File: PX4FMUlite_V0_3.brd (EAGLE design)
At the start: 48.6 x 34.9 mm, 145 parts, among them J2 DF13-4P-1.25V, J201 DF13C-6P-1.25V, J202 DF13C-6P-1.25V, J203 DF13C-6P-1.25V, J3 DF13C-4P-1.25V, J302 DF13C-4P-1.25V, J401 DF13C-4P-1.25V, J403 DF13C-7P-1.25V, J405 DF13C-4P-1.25V, J802 DF13C-3P-1.25V, M3_MOUNT1101 MOUNT-HOLE3.1MM, M3_MOUNT1102 MOUNT-HOLE3.1MM, M3_MOUNT1103 MOUNT-HOLE3.1MM, M3_MOUNT1104 MOUNT-HOLE3.1MM, U101 STM32F4X7VX, U2 MAX3051, U401 MAX3051, X101 3.2x2.5 mm / 24 MHz / 15 ppm

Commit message: More...
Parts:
- moved U$801 6.11 mm to (7.92, 7.11)
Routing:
- net V_SERVO: track 2.50 -> 9.15 mm
- net GND: track 182.0 -> 183.5 mm
- added copper zone on layer 1, net V_SERVO
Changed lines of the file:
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@@
 <layer number="1" name="Top" color="4" fill="1" visible="yes" active="yes"/>
 <layer number="2" name="Ground" color="2" fill="10" visible="no" active="yes"/>
-<layer number="3" name="Horizontal" color="13" fill="15" visible="yes" active="yes"/>
+<layer number="3" name="Horizontal" color="13" fill="15" visible="no" active="yes"/>
 <layer number="4" name="Route4" color="1" fill="4" visible="no" active="no"/>
 <layer number="5" name="Route5" color="4" fill="4" visible="no" active="no"/>
@@
 <layer number="13" name="Route13" color="4" fill="5" visible="no" active="no"/>
 <layer number="14" name="Vertical" color="14" fill="15" visible="no" active="yes"/>
-<layer number="15" name="Power" color="11" fill="15" visible="yes" active="yes"/>
+<layer number="15" name="Power" color="11" fill="15" visible="no" active="yes"/>
 <layer number="16" name="Bottom" color="1" fill="1" visible="yes" active="yes"/>
 <layer number="17" name="Pads" color="2" fill="1" visible="yes" active="yes"/>
 <layer number="18" name="Vias" color="2" fill="1" visible="yes" active="yes"/>
-<layer number="19" name="Unrouted" color="14" fill="1" visible="yes" active="yes"/>
+<layer number="19" name="Unrouted" color="14" fill="1" visible="no" active="yes"/>
 <layer number="20" name="Dimension" color="15" fill="1" visible="yes" active="yes"/>
 <layer number="21" name="tPlace" color="7" fill="1" visible="yes" active="yes"/>
@@
 <attribute name="PARTNO" value="RC0402FR-0710KL" x="87.7824" y="13.9192" size="1.778" layer="27" display="off"/>
 </element>
-<element name="U$801" library="pixhawk2" package="0402-TVS" value="PESD0402-140" x="12.192" y="11.4808" rot="R180">
-<attribute name="PARTNO" value="PESD0402-140" x="12.192" y="10.8712" size="1.778" layer="27" rot="R180" display="off"/>
+<element name="U$801" library="pixhawk2" package="0402-TVS" value="PESD0402-140" x="7.9248" y="7.112" rot="R180">
+<attribute name="PARTNO" value="PESD0402-140" x="7.9248" y="6.5024" size="1.778" layer="27" rot="R180" display="off"/>
 </element>
 <element name="U$14" library="PX4lite" package="3X1RA" value="HEADER-3X1RA" x="10.92" y="9.8552"/>
@@
 <wire x1="22.352" y1="3.6576" x2="20.32" y2="5.6896" width="0.8128" layer="15"/>
 <wire x1="20.32" y1="5.6896" x2="20.32" y2="10.2616" width="0.8128" layer="15"/>
-<wire x1="20.32" y1="10.2616" x2="18.288" y2="10.16" width="0" layer="19" extent="1-16"/>
 <wire x1="57.0992" y1="19.7104" x2="57.0992" y2="20.1168" width="0.6096" layer="15"/>
 <via x="20.32" y="10.2616" extent="1-16" drill="0.3"/>
@@
 <wire x1="18.9992" y1="13.6144" x2="20.2184" y2="13.6144" width="0.8128" layer="14"/>
 <wire x1="20.2184" y1="13.6144" x2="20.4216" y2="13.8176" width="0.8128" layer="14"/>
-<wire x1="20.4216" y1="13.8176" x2="20.4216" y2="18.9992" width="0.8128" layer="14"/>
-<wire x1="20.4216" y1="18.9992" x2="20.0152" y2="19.6088" width="0.8128" layer="14"/>
+<wire x1="20.4216" y1="13.8176" x2="20.4216" y2="19.2024" width="0.8128" layer="14"/>
+<wire x1="20.4216" y1="19.2024" x2="20.0152" y2="19.6088" width="0.8128" layer="14"/>
 <via x="20.0152" y="19.6088" extent="1-16" drill="0.3"/>
 <via x="26.1112" y="19.6088" extent="1-16" drill="0.3"/>
@@
 <via x="19.5072" y="19.1008" extent="1-16" drill="0.3"/>
 <wire x1="20.0152" y1="19.6088" x2="19.5072" y2="19.1008" width="0.6096" layer="3"/>
-<wire x1="13.46" y1="9.8552" x2="12.692" y2="11.4808" width="0" layer="19" extent="1-14"/>
+<wire x1="8.4248" y1="7.112" x2="13.46" y2="9.8552" width="0" layer="19" extent="1-14"/>
 </signal>
 <signal name="N$34">
@@
 <via x="18.796" y="23.876" extent="1-16" drill="0.3"/>
 <via x="18.796" y="22.2504" extent="1-16" drill="0.3"/>
-<via x="18.4912" y="14.3256" extent="1-16" drill="0.3"/>
-<via x="18.9992" y="14.732" extent="1-16" drill="0.3"/>
+<via x="18.3896" y="14.3256" extent="1-16" drill="0.3"/>
+<via x="18.9992" y="14.6304" extent="1-16" drill="0.3"/>
 <via x="18.4912" y="17.1704" extent="1-16" drill="0.3"/>
 <via x="18.8976" y="17.6784" extent="1-16" drill="0.3"/>
@@
 <via x="18.8976" y="20.32" extent="1-16" drill="0.3"/>
 <via x="20.1168" y="26.6192" extent="1-16" drill="0.3"/>
-<wire x1="18.9992" y1="14.732" x2="18.288" y2="14.732" width="0.4064" layer="1"/>
 <wire x1="18.3896" y1="13.0304" x2="18.4152" y2="13.0048" width="0.4064" layer="1"/>
 <wire x1="17.4752" y1="12.8016" x2="18.212" y2="12.8016" width="0.4064" layer="1"/>
@@
 <wire x1="18.3896" y1="11.684" x2="18.3896" y2="12.9792" width="0.4064" layer="1"/>
 <wire x1="18.3896" y1="12.9792" x2="18.4152" y2="13.0048" width="0.4064" layer="1"/>
+<wire x1="18.9992" y1="14.6304" x2="18.796" y2="14.4272" width="0.6096" layer="1"/>
+<wire x1="18.796" y1="14.4272" x2="18.3896" y2="14.4272" width="0.6096" layer="1"/>
+<wire x1="18.3896" y1="14.4272" x2="18.4152" y2="14.4528" width="0.6096" layer="1"/>
+<wire x1="18.4152" y1="14.4528" x2="18.4152" y2="15.9512" width="0.6096" layer="1"/>
+<polygon width="0.1" layer="1">
+<vertex x="17.3736" y="11.9888"/>
+<vertex x="19.1008" y="11.9888"/>
+<vertex x="19.4056" y="12.2936"/>
+<vertex x="19.4056" y="22.2504"/>
+<vertex x="19.1008" y="22.5552"/>
+<vertex x="19.1008" y="24.7904"/>
+<vertex x="20.2184" y="25.908"/>
+<vertex x="20.2184" y="28.2448"/>
+<vertex x="19.9136" y="28.5496"/>
+<vertex x="18.0848" y="28.5496"/>
+<vertex x="17.3736" y="27.8384"/>
+</polygon>
 <wire x1="101.4292" y1="51.6128" x2="99.1696" y2="57.3024" width="0" layer="19" extent="1-1"/>
 <wire x1="67.9624" y1="58.928" x2="99.1696" y2="57.3024" width="0" layer="19" extent="1-1"/>
@@
 <wire x1="46.228" y1="26.7272" x2="46.228" y2="26.416" width="0" layer="19" extent="16-16"/>
 <wire x1="52.5336" y1="12.4968" x2="52.6288" y2="12.192" width="0" layer="19" extent="1-16"/>
-<wire x1="18.4912" y1="22.352" x2="18.796" y2="22.2504" width="0" layer="19" extent="1-1"/>
 <wire x1="20.0152" y1="29.2608" x2="19.7184" y2="29.0576" width="0" layer="19" extent="1-16"/>
 <wire x1="42.4688" y1="33.1152" x2="42.4688" y2="32.7152" width="0" layer="19" extent="16-16"/>
@@
 <wire x1="46.5328" y1="5.6832" x2="46.5328" y2="5.2832" width="0" layer="19" extent="16-16"/>
 <wire x1="46.5328" y1="4.8832" x2="46.5328" y2="5.2832" width="0" layer="19" extent="16-16"/>
-<wire x1="19.403" y1="23.568" x2="19.403" y2="23.968" width="0" layer="19" extent="1-1"/>
-<wire x1="19.403" y1="23.168" x2="19.403" y2="22.768" width="0" layer="19" extent="1-1"/>
 <wire x1="21.736" y1="8.128" x2="21.336" y2="8.128" width="0" layer="19" extent="16-16"/>
 <wire x1="22.253" y1="22.768" x2="21.328" y2="22.868" width="0" layer="19" extent="1-1"/>
@@
 <wire x1="30.93924375" y1="12.139153125" x2="31.10188125" y2="13.716" width="0" layer="19" extent="1-1"/>
 <wire x1="41.09924375" y1="7.97764375" x2="40.0384" y2="6.7056" width="0" layer="19" extent="1-1"/>
-<wire x1="11.692" y1="11.4808" x2="10.92" y2="9.8552" width="0" layer="19" extent="1-1"/>
 <wire x1="27.948" y1="24.6888" x2="28.948" y2="22.9616" width="0" layer="19" extent="1-1"/>
 <wire x1="49.9872" y1="23.5712" x2="52.324" y2="23.6728" width="0" layer="19" extent="16-16"/>
@@
 <wire x1="26.7208" y1="27.948" x2="27.948" y2="24.6888" width="0" layer="19" extent="1-1"/>
 <wire x1="46.4312" y1="11.9888" x2="47.926" y2="8.7536" width="0" layer="19" extent="1-1"/>
+<wire x1="7.4248" y1="7.112" x2="10.92" y2="9.8552" width="0" layer="19" extent="1-1"/>
 <wire x1="17.9752" y1="34.544" x2="22.8026" y2="35.5802" width="0" layer="19" extent="1-1"/>
 <wire x1="15.8784" y1="36.0818" x2="17.9752" y2="34.544" width="0" layer="19" extent="1-16"/>
@@
 <contactref element="J1" pad="PWR_S1"/>
 <contactref element="J1" pad="PWR_S3"/>
-<wire x1="13.462" y1="30.9372" x2="100.1696" y2="55.2704" width="0" layer="19" extent="1-1"/>
-<wire x1="13.462" y1="28.3972" x2="13.462" y2="30.9372" width="0" layer="19" extent="1-1"/>
-<wire x1="13.462" y1="25.8572" x2="13.462" y2="28.3972" width="0" layer="19" extent="1-1"/>
-<wire x1="13.462" y1="23.3172" x2="13.462" y2="25.8572" width="0" layer="19" extent="1-1"/>
-<wire x1="13.462" y1="20.7772" x2="13.462" y2="23.3172" width="0" layer="19" extent="1-1"/>
-<wire x1="13.462" y1="18.2372" x2="13.462" y2="20.7772" width="0" layer="19" extent="1-1"/>
-<wire x1="13.462" y1="15.6972" x2="13.462" y2="18.2372" width="0" layer="19" extent="1-1"/>
-<wire x1="13.462" y1="13.1572" x2="13.462" y2="15.6972" width="0" layer="19" extent="1-1"/>
 <wire x1="19.8972" y1="8.3312" x2="18.6944" y2="8.3312" width="0.8128" layer="1"/>
 <wire x1="18.6944" y1="8.3312" x2="17.78" y2="9.2456" width="0.8128" layer="1"/>
-<wire x1="17.78" y1="9.2456" x2="13.462" y2="13.1572" width="0" layer="19" extent="1-16"/>
+<wire x1="17.78" y1="9.2456" x2="17.4752" y2="9.5504" width="0.4064" layer="1"/>
+<wire x1="17.4752" y1="9.5504" x2="17.4752" y2="10.4648" width="0.4064" layer="1"/>
+<wire x1="17.4752" y1="10.4648" x2="16.4592" y2="11.4808" width="0.4064" layer="1"/>
+<wire x1="16.4592" y1="11.4808" x2="14.8336" y2="11.4808" width="0.4064" layer="1"/>
+<wire x1="14.8336" y1="11.4808" x2="13.462" y2="12.8524" width="0.4064" layer="1"/>
+<wire x1="13.462" y1="12.8524" x2="13.462" y2="13.1572" width="0.4064" layer="1"/>
+<polygon width="0.1" layer="1" thermals="no">
+<vertex x="18.6944" y="7.9248"/>
+<vertex x="15.4432" y="7.9248"/>
+<vertex x="14.5288" y="8.7376"/>
+<vertex x="14.5288" y="10.0584"/>
+<vertex x="13.1064" y="11.4808"/>
+<vertex x="13.1064" y="12.4968"/>
+<vertex x="13.5128" y="12.9032"/>
+<vertex x="14.3256" y="12.9032"/>
+<vertex x="15.24" y="11.8872"/>
+<vertex x="16.3576" y="11.8872"/>
+<vertex x="18.6944" y="9.5504"/>
+</polygon>
+<polygon width="0.1" layer="1" thermals="no">
+<vertex x="12.2936" y="31.9024"/>
+<vertex x="14.8336" y="31.9024"/>
+<vertex x="14.8336" y="12.7"/>
+<vertex x="14.1224" y="11.9888"/>
+<vertex x="12.8016" y="11.9888"/>
+<vertex x="12.3952" y="12.3952"/>
+<vertex x="12.2936" y="12.4968"/>
+</polygon>
+<wire x1="13.462" y1="30.9372" x2="100.1696" y2="55.2704" width="0" layer="19" extent="1-1"/>
 </signal>
 </signals>

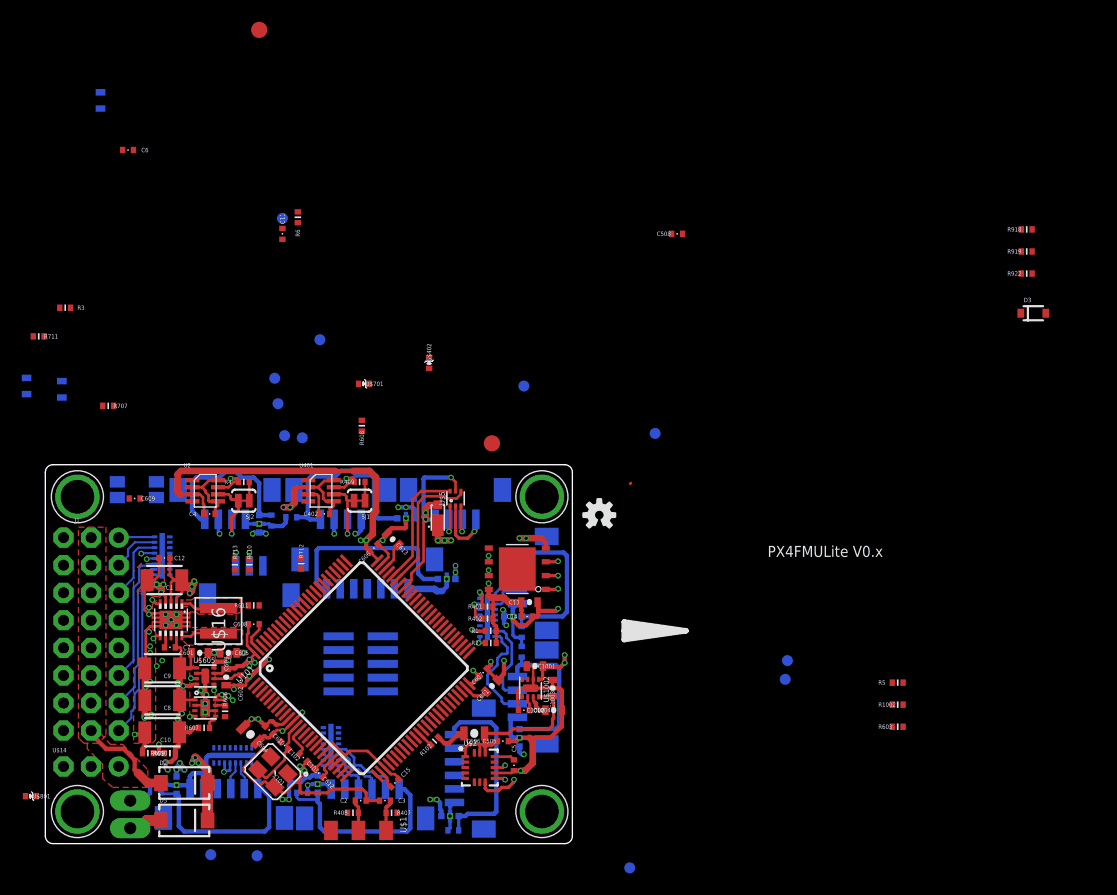
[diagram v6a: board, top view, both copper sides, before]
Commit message: Fitting pull-up down resistors in
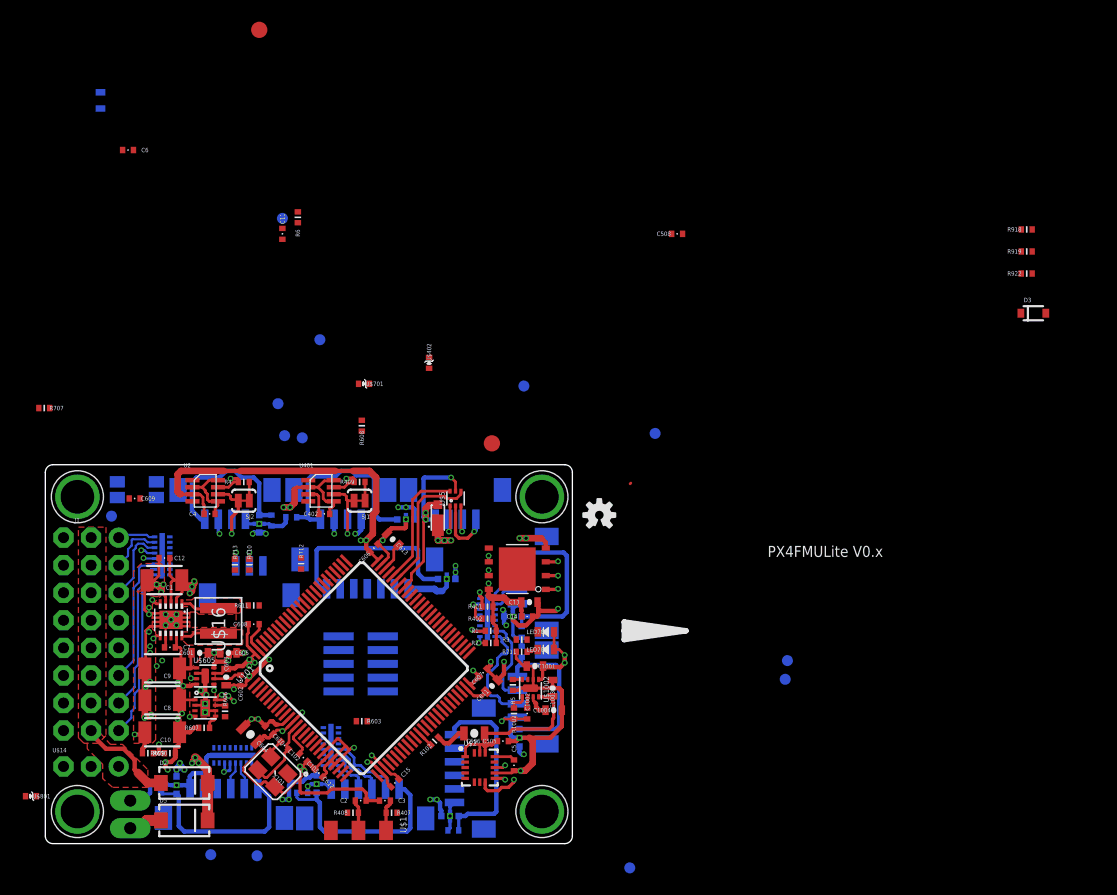
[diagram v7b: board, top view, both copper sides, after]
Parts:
- moved LED704 53.7 mm to (55.4, 20.6), flipped to the top, turned to 0 degrees
- moved R711 53.1 mm to (53.1, 20.4), turned to 0 degrees
- moved R3 52.0 mm to (53.1, 21.5), turned to 0 degrees
- moved LED701 49.9 mm to (55.4, 22.3), flipped to the top, turned to 0 degrees
- moved R603 49.4 mm to (38.4, 14.0), turned to 180 degrees
- moved R5 35.5 mm to (52.3, 17.4), turned to 90 degrees
- moved R1002 35.4 mm to (52.4, 14.7), turned to 90 degrees
- moved FMU-BOOT0 19.7 mm to (15.3, 32.9)
- moved R707 5.90 mm to (9.14, 42.9)
- moved C1002 0.43 mm to (53.6, 14.7), turned to 270 degrees
- moved L202 0.10 mm to (34.2, 8.23)
- moved L403 0.10 mm to (42.5, 32.6)
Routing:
- net GND: track 183.5 -> 191.6 mm, vias 35 -> 37
- net VDD_5V: track 82.1 -> 84.9 mm
- net VDD_3V3_SENSORS_EN: track 0.00 -> 1.71 mm
- net N$7: track 0.00 -> 1.07 mm
- net VDD_3V3_PERIPH_EN: track 0.00 -> 0.88 mm
- net FMU-VDD_3V3: track 76.1 -> 76.9 mm, vias 9 -> 11
- net N$78: track 6.40 -> 6.95 mm
- net N$79: track 4.55 -> 5.07 mm

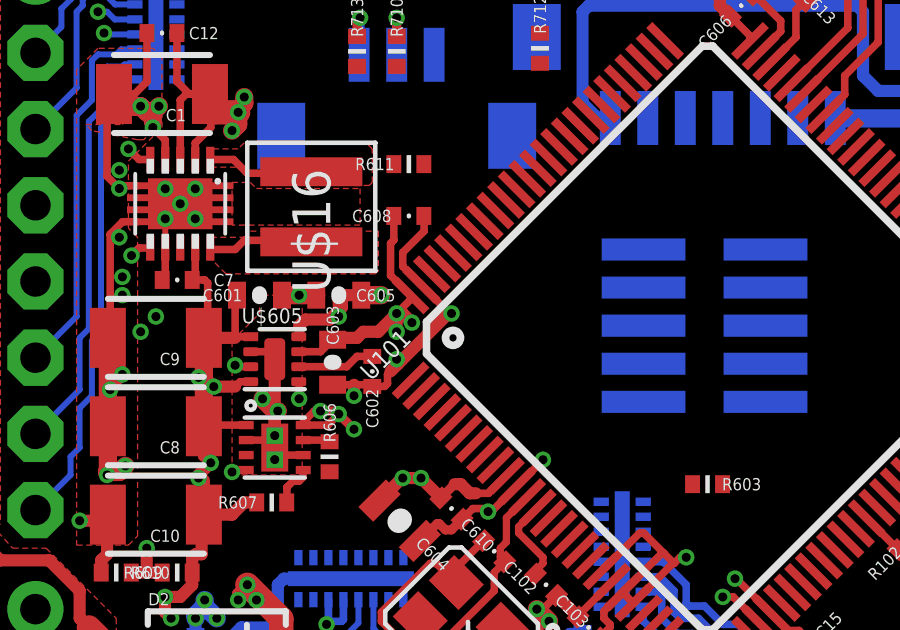
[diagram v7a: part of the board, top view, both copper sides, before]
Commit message: Moved gps to uart 7 to make room for using timer1/5 for IO
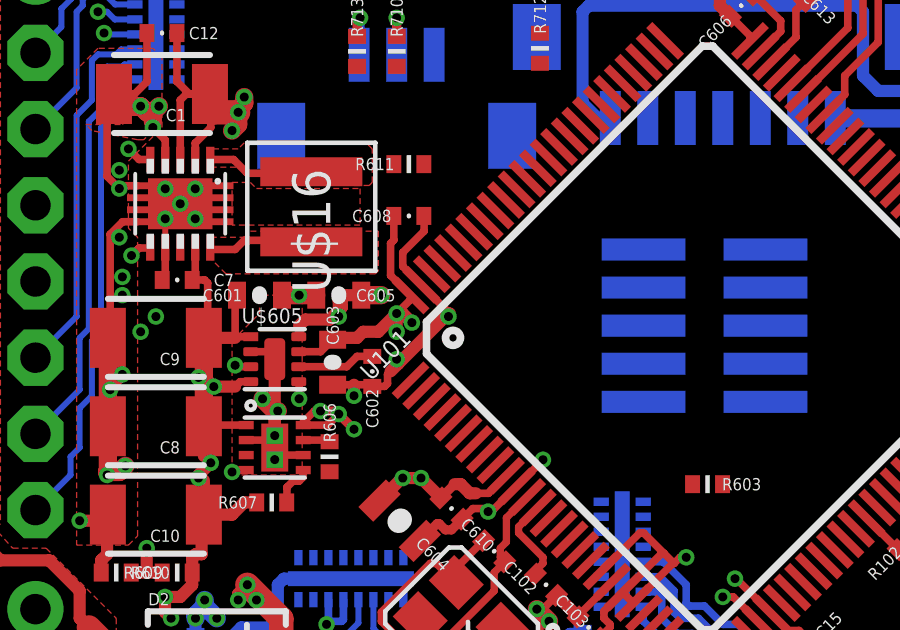
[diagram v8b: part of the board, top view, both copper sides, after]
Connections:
- removed net !VDD_BRICK_VALID: U101.91
- net !VDD_5V_VALID: now also U101.91
- net FMU-UART4_RX: no longer L3.P$5
- net FMU-UART4_TX: no longer L3.P$6
- net FMU-UART7_RX: now also L3.P$5
- net FMU-UART7_TX: now also L3.P$6
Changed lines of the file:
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@@
 <signal name="FMU-UART4_TX">
 <contactref element="U101" pad="23"/>
-<contactref element="L3" pad="P$6"/>
-<wire x1="27.2676" y1="11.5712" x2="36.283478125" y2="9.705209375" width="0" layer="19" extent="1-16"/>
 </signal>
 <signal name="FMU-UART4_RX">
 <contactref element="U101" pad="24"/>
-<contactref element="L3" pad="P$5"/>
-<wire x1="26.7676" y1="11.5712" x2="36.63703125" y2="9.35165625" width="0" layer="19" extent="1-16"/>
 </signal>
 <signal name="FMU-UART7_TX">
 <contactref element="U101" pad="39"/>
+<contactref element="L3" pad="P$6"/>
+<wire x1="27.2676" y1="11.5712" x2="44.41520625" y2="13.594296875" width="0" layer="19" extent="1-16"/>
 </signal>
 <signal name="FMU-UART7_RX">
 <contactref element="U101" pad="38"/>
+<contactref element="L3" pad="P$5"/>
+<wire x1="26.7676" y1="11.5712" x2="44.061653125" y2="13.24074375" width="0" layer="19" extent="1-16"/>
 </signal>
 <signal name="FMU-UART8_TX">
@@
 <wire x1="43.5864" y1="31.6992" x2="44.6024" y2="30.6832" width="0.8128" layer="15"/>
 <wire x1="44.6024" y1="30.6832" x2="46.6344" y2="30.6832" width="0.6096" layer="15"/>
-</signal>
-<signal name="!VDD_BRICK_VALID">
-<contactref element="U101" pad="91"/>
 </signal>
 <signal name="!VDD_SERVO_VALID">
@@
 <via x="24.7904" y="20.32" extent="1-16" drill="0.3"/>
 <via x="26.6192" y="16.9672" extent="1-16" drill="0.3"/>
-<via x="29.8704" y="19.7104" extent="1-16" drill="0.3"/>
+<via x="29.7688" y="19.6088" extent="1-16" drill="0.3"/>
 <wire x1="33.8392" y1="8.2296" x2="33.6296" y2="8.2296" width="0.254" layer="16"/>
 <wire x1="33.6296" y1="8.2296" x2="33.4264" y2="8.0264" width="0.254" layer="16"/>
@@
 <wire x1="28.0416" y1="18.1864" x2="28.0416" y2="18.0848" width="0.4064" layer="1"/>
 <wire x1="28.0416" y1="18.0848" x2="28.0924" y2="18.034" width="0.4064" layer="1"/>
-<wire x1="29.7688" y1="19.7104" x2="29.8704" y2="19.7104" width="0.4064" layer="1"/>
 <wire x1="19.9136" y1="8.4248" x2="19.0928" y2="8.4248" width="0.4064" layer="16"/>
 <wire x1="19.0928" y1="8.4248" x2="18.8976" y2="8.2296" width="0.4064" layer="16"/>
@@
 <wire x1="54.1996" y1="17.3188" x2="53.9496" y2="17.0688" width="0.254" layer="1"/>
 <wire x1="28.85885625" y1="20.665365625" x2="29.813821875" y2="19.7104" width="0.254" layer="1"/>
-<wire x1="29.813821875" y1="19.7104" x2="29.8704" y2="19.7104" width="0.254" layer="1"/>
 <wire x1="52.6368" y1="20.4216" x2="52.6288" y2="20.4136" width="0.254" layer="1"/>
 <wire x1="52.6288" y1="20.4136" x2="52.6288" y2="19.812" width="0.254" layer="1"/>
@@
 <wire x1="52.84" y1="16.8736" x2="53.0352" y2="17.0688" width="0.3048" layer="1"/>
 <wire x1="53.0352" y1="17.0688" x2="53.9496" y2="17.0688" width="0.3048" layer="1"/>
+<wire x1="29.813821875" y1="19.7104" x2="29.7688" y2="19.7104" width="0.4064" layer="1"/>
+<wire x1="29.7688" y1="19.7104" x2="29.7688" y2="19.6088" width="0.4064" layer="1"/>
 </signal>
 <signal name="N$4">
@@
 <via x="19.1008" y="25.1968" extent="1-16" drill="0.3"/>
 <wire x1="19.1008" y1="25.1968" x2="19.304" y2="24.9936" width="0.254" layer="16"/>
-<wire x1="19.1008" y1="25.1968" x2="32.512" y2="59.952" width="0" layer="19" extent="1-1"/>
+<contactref element="U101" pad="91"/>
+<wire x1="31.687284375" y1="23.49379375" x2="32.512" y2="59.952" width="0" layer="19" extent="1-1"/>
+<wire x1="19.828" y1="24.843" x2="31.687284375" y2="23.49379375" width="0" layer="19" extent="1-1"/>
 </signal>
 <signal name="FMU-CH7">
